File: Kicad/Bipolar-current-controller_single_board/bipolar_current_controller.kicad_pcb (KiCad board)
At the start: 4 copper layers, 114.3 x 127 mm, 131 parts, among them J1 Error signal, J2 Set point, J4 Monitor, J5 Conn_02x04_Counter_Clockwise, J6 Enable, J7 P-MOS, J8 N-MOS, J9 Shunt resistor, P1 CONN_01X03, U1 AD8421, U11 LM338, U12 LM337_TO220, U13 LM7915, U14 uA7815, U15 LM7905, U16 LM7805, U17 TL1963A, U18 LM337_TO220, U19 FOD8482TR2, U2 AD8421, U3 AD8421, U4 OPA388, U5 LT1363, U6 LT1363, U7 BUF634A, U8 BUF634A

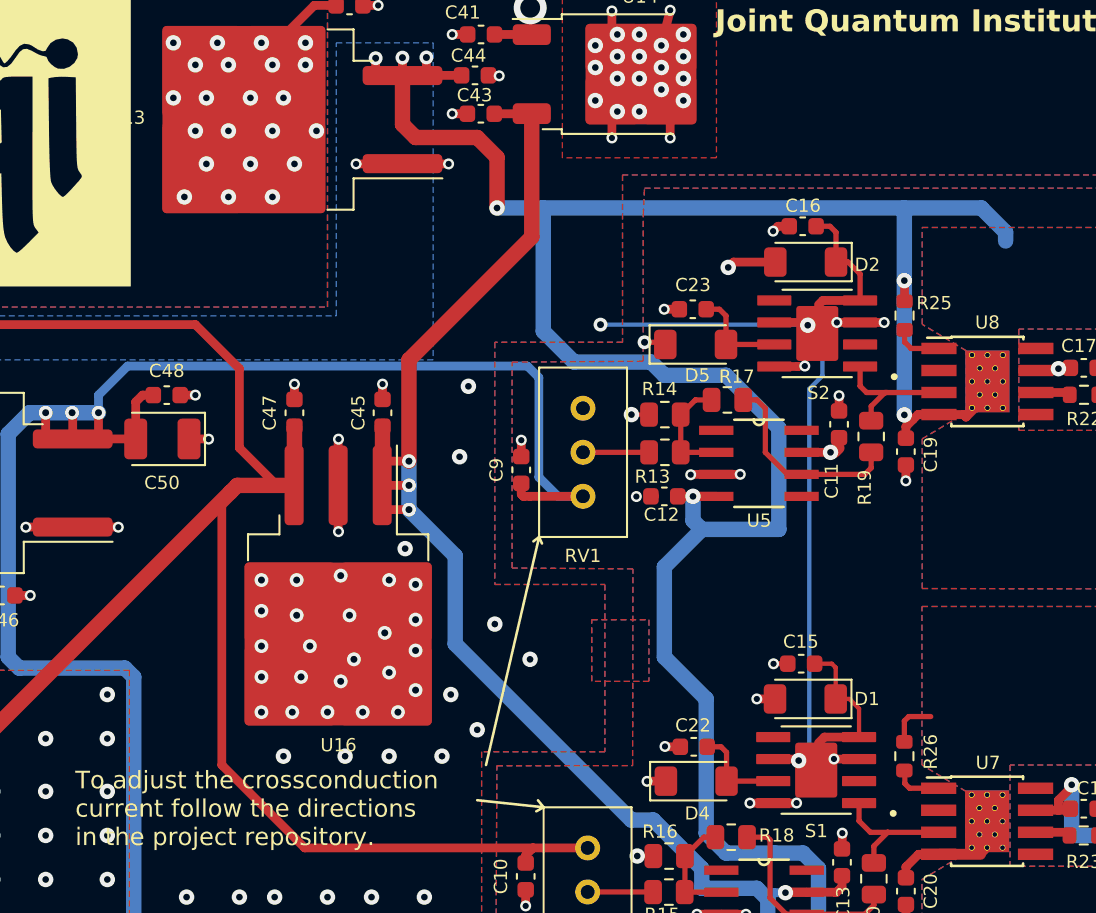
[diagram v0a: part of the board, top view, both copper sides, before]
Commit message: Corrections of the design after modification of package
1) The switches were short circuited, I had to remove offending via connections from under the packages.
2) F.Fab larer has been cleaned up a bit: this will allow for printing a mounting diagram.
3) In the schematic the GND label has been substituted with teh GND symbol.
4) Added comments about J5 connector.
5) Removed .~lock.BOM.csv# that was committed by mistake
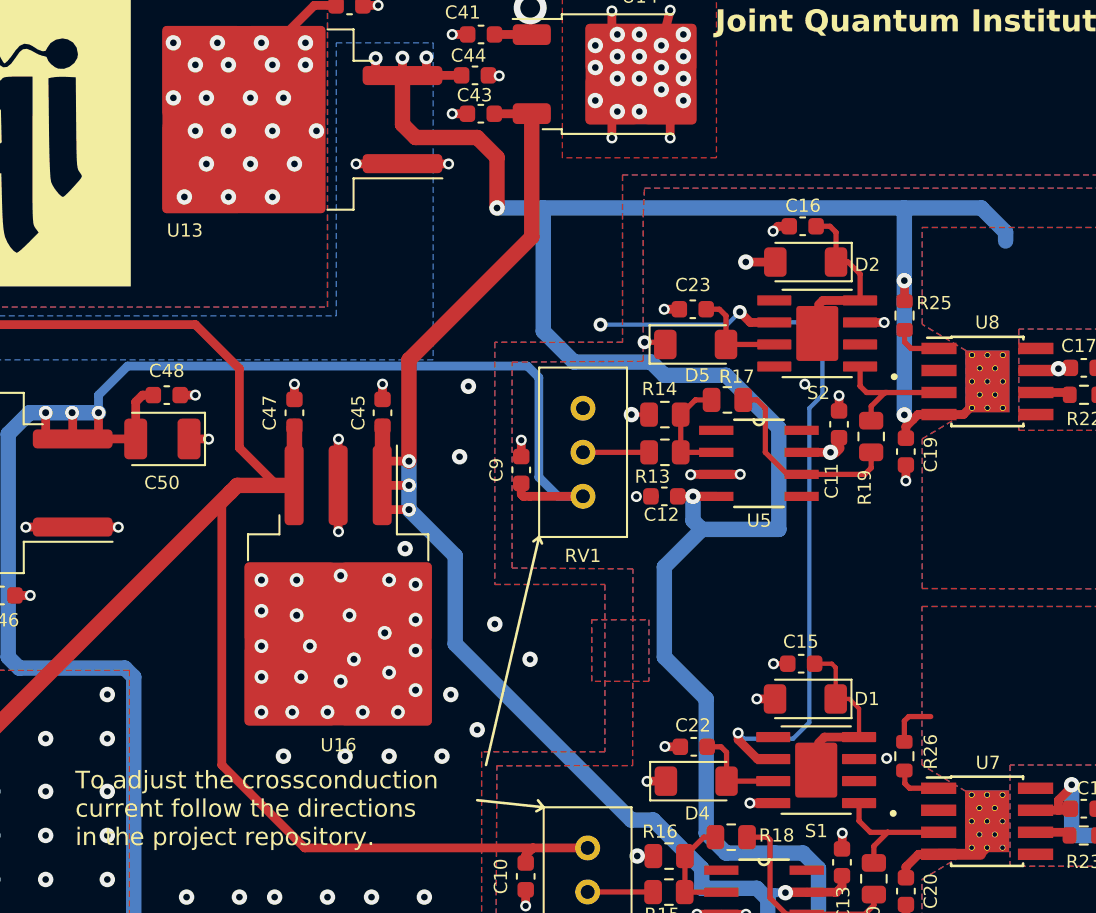
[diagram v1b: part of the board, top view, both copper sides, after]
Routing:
- net GND: track 97.6 -> 92.1 mm, vias 233 -> 231
- net Digital_control: track 123.6 -> 126.7 mm
- net -15V: track 164.3 -> 164.8 mm
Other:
- board text removed: "ADD RF filters to some of the INAs Change footprints of BUF: they run very hot! If swapping the connectors help go fo it! leave space for optocoupler for digital enable"

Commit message: Swap P-MOS and N-MOS labels
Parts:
- J7: value P-MOS -> N-MOS
- J8: value N-MOS -> P-MOS
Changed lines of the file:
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@@
         (effects (font (size 0.762 0.762) (thickness 0.1016)))
     )
-    (fp_text value "P-MOS" (at 8.591686 -1.931123 90) (layer "F.SilkS")
+    (fp_text value "N-MOS" (at 8.088138 -2.017158 90) (layer "F.SilkS")
         (effects (font (size 1.27 1.27) (thickness 0.254)))
     )
@@
         (effects (font (size 0.762 0.762) (thickness 0.1016)))
     )
-    (fp_text value "N-MOS" (at -7.62 -2.032 90) (layer "F.SilkS")
+    (fp_text value "P-MOS" (at -5.549731 -2.21211 90) (layer "F.SilkS")
         (effects (font (size 1.27 1.27) (thickness 0.254)))
     )
